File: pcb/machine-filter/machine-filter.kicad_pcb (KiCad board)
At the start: 2 copper layers, 150 x 107 mm, 162 parts, among them J1 PJ398SM, J10 PJ398SM, J11 PJ398SM, J12 PJ398SM, J13 EURO PWR 2x5, J14 EXPANSION 2x4, J15 TF-01A, J2 PJ398SM, J3 PJ398SM, J4 PJ398SM, J5 PJ398SM, J6 PJ398SM, J7 PJ398SM, J8 PJ398SM, J9 PJ398SM, U1 LMV324, U2 LMV324, U3 TL072, U4 TL072, U5 LM4040-10, U6 74HC4051, U7 LM324, U8 LM324

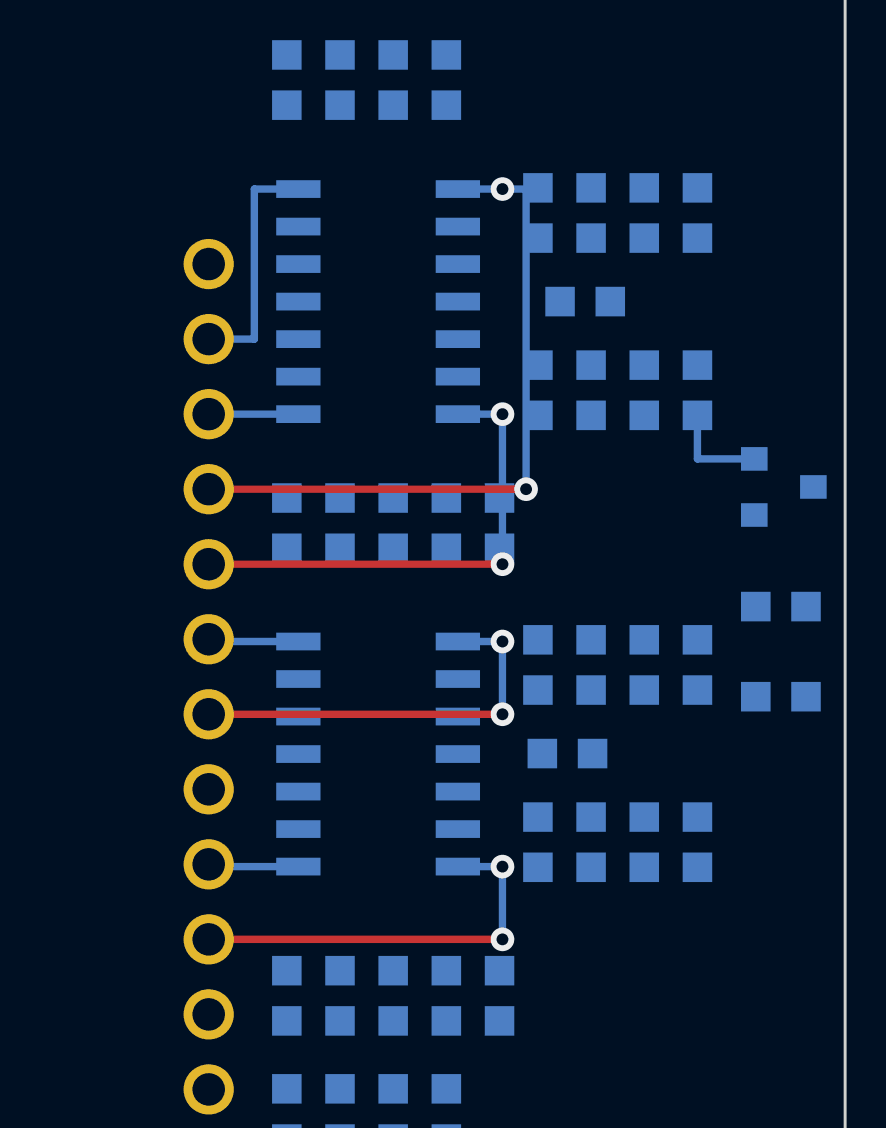
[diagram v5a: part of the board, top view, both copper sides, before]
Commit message: U1/U2 1.5 mm further from the Seed3 (d), C20/C21 with them; ADC traces redrawn; leftover vias removed
DRC: 0 problems (44 clashes with untraced minor parts ignored).

Co-Authored-By: Claude Opus 5.5 <noreply@anthropic.com>
Claude-Session: https://claude.ai/code/session_01Cf5qNBi3oNHhbCjPHvswth
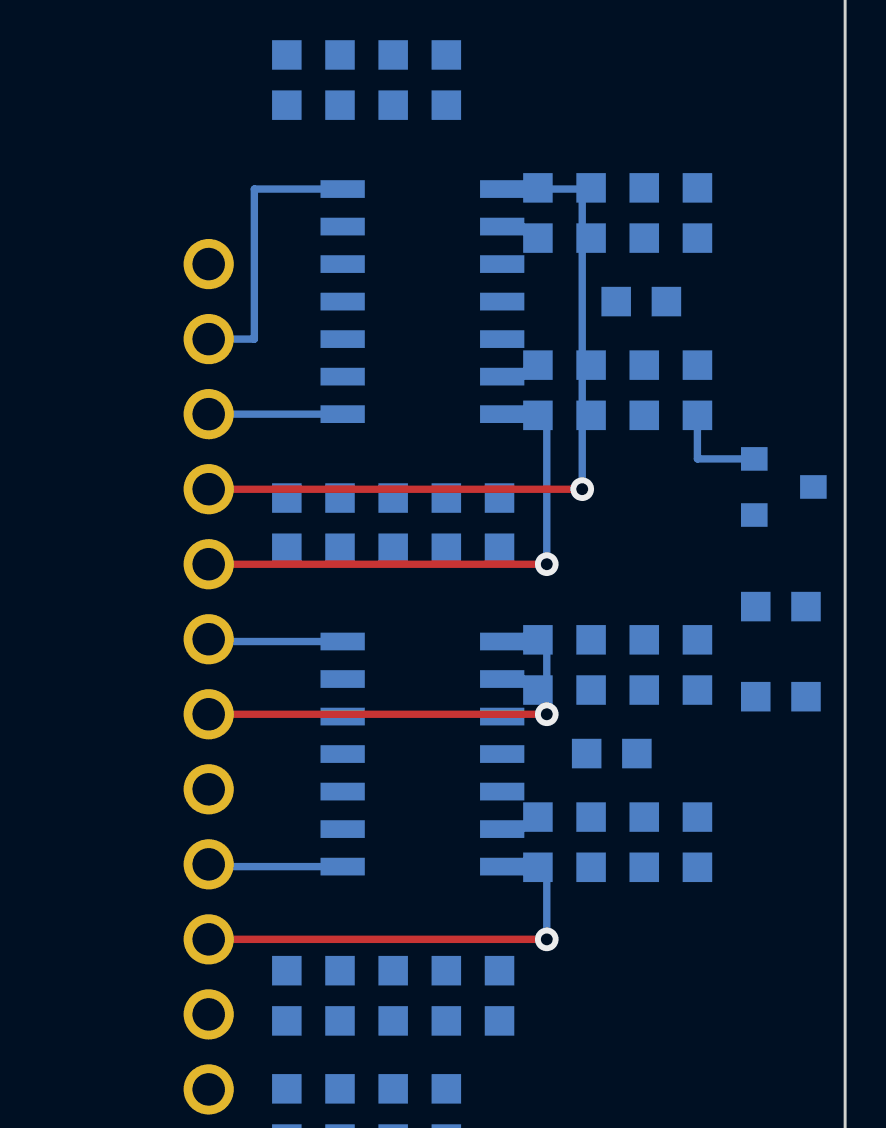
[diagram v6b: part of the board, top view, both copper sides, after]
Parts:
- moved C21 1.90 mm to (243.5, 92.5)
- moved C20 1.50 mm to (242.5, 107.8)
- moved U1 1.50 mm to (236.1, 107.8)
- moved U2 1.50 mm to (236.1, 92.5)
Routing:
- net ADC_LPRES: track 23.2 -> 25.5 mm, vias 2 -> 1
- net ADC_WIDTH: track 3.03 -> 4.53 mm
- net ADC_SRR: track 13.9 -> 15.4 mm, vias 2 -> 1
- net ADC_HPRES: track 8.11 -> 9.61 mm
- net ADC_EQG: track 3.03 -> 4.53 mm
- net ADC_EQF: track 16.5 -> 18.0 mm, vias 2 -> 1
- net ADC_DIST: track 13.9 -> 15.4 mm, vias 2 -> 1
- net ADC_BASE: track 3.04 -> 4.53 mm
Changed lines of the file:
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@@
 	(footprint "filter-module:SOIC-14_3.9x8.65mm_Pitch1.27mm"
 		(layer "B.Cu")
-		(at 234.6 92.493)
+		(at 236.1 92.493)
 		(descr "16-Lead Plastic Small Outline (SL) - Narrow, 3.90 mm Body [SOIC] (see Microchip Packaging Specification 00000049BS.pdf)")
 		(tags "SOIC 1.27")
@@
 	(footprint "filter-module:C_0603"
 		(layer "B.Cu")
-		(at 241 107.8)
+		(at 242.5 107.8)
 		(descr "Capacitor SMD 0603, reflow soldering, AVX (see smccp.pdf)")
 		(tags "capacitor 0603 C0603")
@@
 	(footprint "filter-module:SOIC-14_3.9x8.65mm_Pitch1.27mm"
 		(layer "B.Cu")
-		(at 234.6 107.81)
+		(at 236.1 107.81)
 		(descr "16-Lead Plastic Small Outline (SL) - Narrow, 3.90 mm Body [SOIC] (see Microchip Packaging Specification 00000049BS.pdf)")
 		(tags "SOIC 1.27")
@@
 	(footprint "filter-module:C_0603"
 		(layer "B.Cu")
-		(at 241.6 92.5)
+		(at 243.5 92.5)
 		(descr "Capacitor SMD 0603, reflow soldering, AVX (see smccp.pdf)")
 		(tags "capacitor 0603 C0603")
@@
 	)
 	(segment
-		(start 231.89 111.627)
+		(start 233.39 111.627)
 		(end 228.855 111.627)
 		(width 0.25)
@@
 	)
 	(segment
-		(start 231.89 96.310001)
+		(start 233.39 96.31)
 		(end 228.855 96.31)
 		(width 0.25)
@@
 	)
 	(segment
-		(start 239.6 98.85)
+		(start 241.5 98.85)
 		(end 228.855 98.85)
 		(width 0.25)
@@
 	)
 	(via
-		(at 238.8 88.69)
+		(at 241.5 98.85)
 		(size 0.8)
 		(drill 0.4)
@@
 		(net "ADC_LPRES")
 	)
-	(via
-		(at 239.6 98.85)
-		(size 0.8)
-		(drill 0.4)
-		(layers "F.Cu" "B.Cu")
-		(net "ADC_LPRES")
-	)
-	(segment
-		(start 239.6 88.69)
-		(end 239.6 98.85)
-		(width 0.25)
-		(layer "B.Cu")
-		(net "ADC_LPRES")
-	)
 	(segment
-		(start 238.8 88.69)
-		(end 239.6 88.69)
+		(start 241.5 88.69)
+		(end 241.5 98.85)
 		(width 0.25)
 		(layer "B.Cu")
@@
 	)
 	(segment
-		(start 237.29 88.69)
-		(end 238.8 88.69)
+		(start 238.79 88.69)
+		(end 241.5 88.69)
 		(width 0.25)
 		(layer "B.Cu")
@@
 	)
 	(segment
-		(start 231.89 88.69)
-		(end 230.4 88.69)
+		(start 230.4 88.69)
+		(end 230.4 93.77)
 		(width 0.25)
 		(layer "B.Cu")
@@
 	)
 	(segment
-		(start 230.4 88.69)
-		(end 230.4 93.77)
+		(start 230.4 93.77)
+		(end 228.855 93.77)
 		(width 0.25)
 		(layer "B.Cu")
@@
 	)
 	(segment
-		(start 230.4 93.77)
-		(end 228.855 93.77)
+		(start 233.39 88.69)
+		(end 230.4 88.69)
 		(width 0.25)
 		(layer "B.Cu")
@@
 	)
 	(segment
-		(start 238.8 101.39)
+		(start 240.3 101.39)
 		(end 228.855 101.39)
 		(width 0.25)
@@
 	)
 	(via
-		(at 238.8 101.39)
-		(size 0.8)
-		(drill 0.4)
-		(layers "F.Cu" "B.Cu")
-		(net "ADC_EQF")
-	)
-	(via
-		(at 238.8 96.31)
+		(at 240.3 101.39)
 		(size 0.8)
 		(drill 0.4)
@@
 	)
 	(segment
-		(start 237.29 96.31)
-		(end 238.8 96.31)
+		(start 238.79 96.31)
+		(end 240.3 96.31)
 		(width 0.25)
 		(layer "B.Cu")
@@
 	)
 	(segment
-		(start 238.8 96.31)
-		(end 238.8 101.39)
+		(start 240.3 96.31)
+		(end 240.3 101.39)
 		(width 0.25)
 		(layer "B.Cu")
@@
 	)
 	(segment
-		(start 231.89 104.007)
+		(start 233.39 104.007)
 		(end 228.855 104.007)
 		(width 0.25)
@@
 	)
 	(segment
-		(start 238.8 106.47)
+		(start 240.3 106.47)
 		(end 228.855 106.47)
 		(width 0.25)
@@
 	)
 	(via
-		(at 238.8 106.47)
-		(size 0.8)
-		(drill 0.4)
-		(layers "F.Cu" "B.Cu")
-		(net "ADC_DIST")
-	)
-	(via
-		(at 238.8 104.007)
+		(at 240.3 106.47)
 		(size 0.8)
 		(drill 0.4)
@@
 	)
 	(segment
-		(start 237.29 104.007)
-		(end 238.8 104.007)
+		(start 238.79 104.007)
+		(end 240.3 104.007)
 		(width 0.25)
 		(layer "B.Cu")
@@
 	)
 	(segment
-		(start 238.8 104.007)
-		(end 238.8 106.47)
+		(start 240.3 104.007)
+		(end 240.3 106.47)
 		(width 0.25)
 		(layer "B.Cu")
@@
 	)
 	(segment
-		(start 238.8 114.09)
+		(start 240.3 114.09)
 		(end 228.855 114.09)
 		(width 0.25)
@@
 	)
 	(via
-		(at 238.8 114.09)
-		(size 0.8)
-		(drill 0.4)
-		(layers "F.Cu" "B.Cu")
-		(net "ADC_SRR")
-	)
-	(via
-		(at 238.8 111.627)
+		(at 240.3 114.09)
 		(size 0.8)
 		(drill 0.4)
@@
 	)
 	(segment
-		(start 238.8 111.627)
-		(end 238.8 114.09)
+		(start 238.79 111.627)
+		(end 240.3 111.627)
 		(width 0.25)
 		(layer "B.Cu")
@@
 	)
 	(segment
-		(start 237.29 111.627)
-		(end 238.8 111.627)
+		(start 240.3 111.627)
+		(end 240.3 114.09)
 		(width 0.25)
 		(layer "B.Cu")

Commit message: Op-amps rotated 90 deg each toward the Seed3 (d); J13 upright with its block re-packed; J14 upright by the edge; traces redrawn
- U2/U1 clockwise, U3/U4 counter-clockwise (by which keeps more Seed3-connected
  pins near it); konnect_place.py picks the KiCad angle by where pad 1 lands.
- Eight ADC traces redrawn; old vias removed with kicad-python (by net, and one
  re-netted via by position).
- Power block packed beside the upright header (fits: 31 x 23 mm).
- J14 upright at x 64.6; USB D-/D+ redrawn.
DRC: 0 problems (50 clashes with untraced minor parts ignored).

Co-Authored-By: Claude Opus 5.5 <noreply@anthropic.com>
Claude-Session: https://claude.ai/code/session_01Cf5qNBi3oNHhbCjPHvswth
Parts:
- moved C1 20.0 mm to (207.2, 136.9)
- moved D10 20.0 mm to (201.7, 136.9)
- moved C3 14.0 mm to (202.3, 149.0)
- moved D11 14.0 mm to (196.8, 149.0)
- moved FB1 11.5 mm to (196.2, 137.0)
- moved J14 8.49 mm to (244.6, 133.1), turned to 180 degrees
- moved J13 8.10 mm to (188.0, 146.7), turned to 180 degrees
- moved C2 8.02 mm to (199.2, 143.0)
- moved FB2 8.02 mm to (207.1, 140.4)
- moved C4 4.68 mm to (199.2, 155.0)
- moved C20 1.00 mm to (243.5, 107.8)
- turned U1 to -90 degrees
- turned U2 to -90 degrees
- turned U3 to 90 degrees
- turned U4 to 90 degrees
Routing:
- net ADC_EQG: track 4.53 -> 14.4 mm, vias 0 -> 1
- net ADC_SRR: track 15.4 -> 7.02 mm, vias 1 -> 0
- net ADC_EQF: track 18.0 -> 9.63 mm, vias 1 -> 0
- net /Main: Daisy Seed3/USB_DP: track 11.5 -> 19.6 mm
- net ADC_HPRES: track 9.61 -> 17.2 mm, vias 0 -> 1
- net ADC_LPRES: track 25.5 -> 18.1 mm
- net ADC_BASE: track 4.53 -> 9.95 mm
- net ADC_WIDTH: track 4.53 -> 9.88 mm
- net ADC_DIST: track 15.4 -> 18.5 mm
- net Net-(FB1-Pad1): track 10.6 -> 13.2 mm

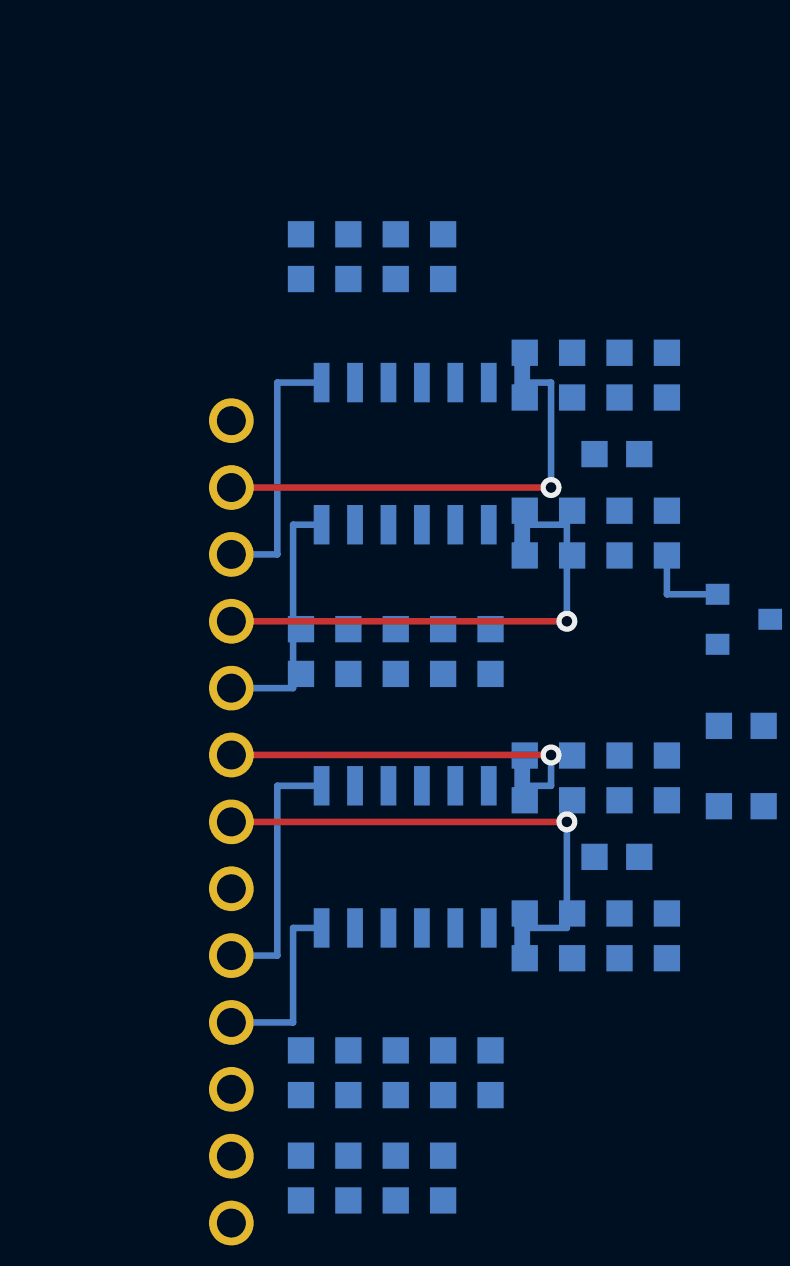
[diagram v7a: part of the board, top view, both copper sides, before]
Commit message: Input resistors R10/R13 (BASE), R18 (HP RES), R14/R17 (WIDTH) in line with their op-amp pins; straight traces (d)
Co-Authored-By: Claude Opus 5.5 <noreply@anthropic.com>
Claude-Session: https://claude.ai/code/session_01Cf5qNBi3oNHhbCjPHvswth
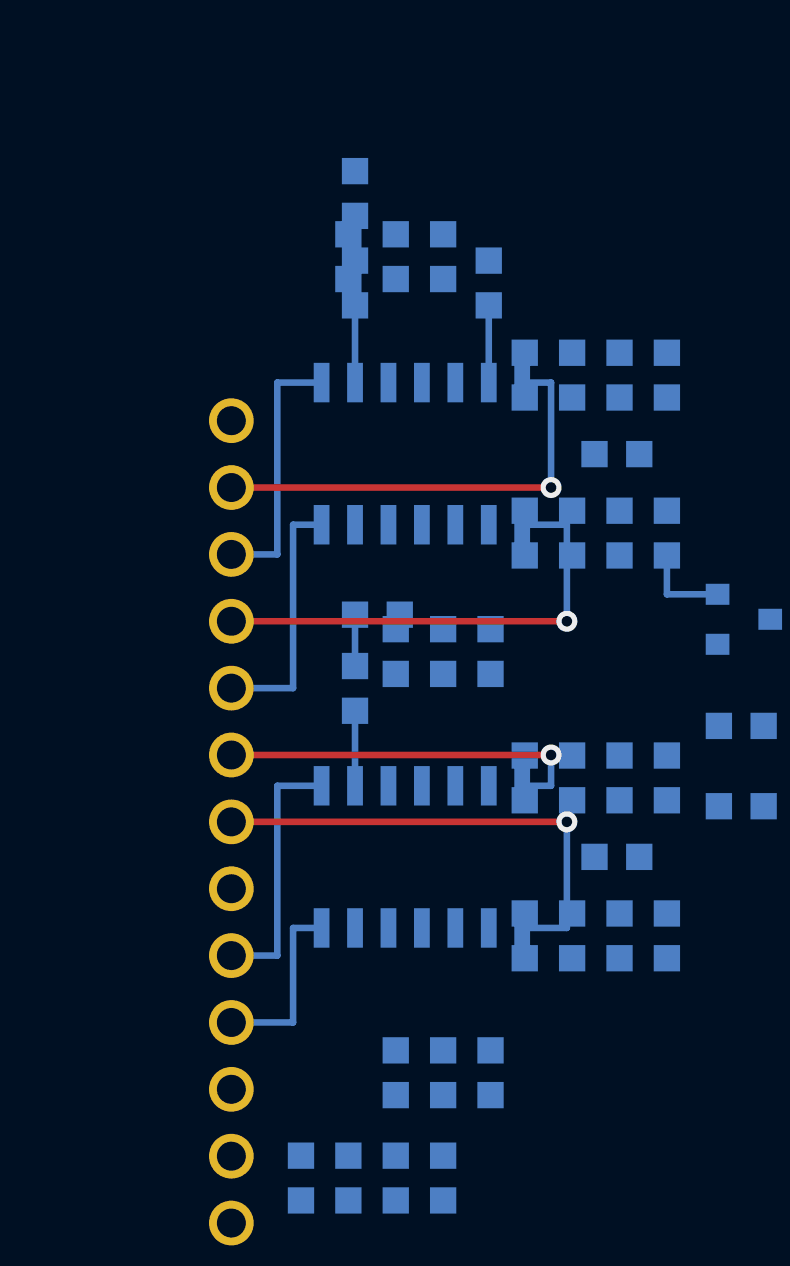
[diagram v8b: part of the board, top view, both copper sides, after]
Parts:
- moved R14 17.6 mm to (234.4, 98.6), turned to 180 degrees
- moved R10 17.5 mm to (233.6, 82.6)
- moved R17 14.6 mm to (233.6, 101.4), turned to -90 degrees
- moved R13 14.0 mm to (233.6, 86.0)
- moved R18 7.20 mm to (238.6, 86.0)
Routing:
- net Net-(U2B--): track 0.00 -> 2.93 mm
- net Net-(U2A--): track 0.00 -> 2.93 mm
- net Net-(U1A--): track 0.00 -> 2.85 mm
- net Net-(R14-Pad2): track 0.00 -> 1.95 mm
- net Net-(R10-Pad2): track 0.00 -> 1.70 mm
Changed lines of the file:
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@@
 	(footprint "filter-module:R_0603"
 		(layer "B.Cu")
-		(at 231.5 100 -90)
+		(at 233.553 82.6 -90)
 		(descr "Resistor SMD 0603, reflow soldering, Vishay (see dcrcw.pdf)")
 		(tags "resistor 0603")
@@
 	(footprint "filter-module:R_0603"
 		(layer "B.Cu")
-		(at 231.5 116 90)
+		(at 234.403 98.6 180)
 		(descr "Resistor SMD 0603, reflow soldering, Vishay (see dcrcw.pdf)")
 		(tags "resistor 0603")
 		(property "Reference" "R14"
-			(at 0 1.449999 270)
+			(at 0 1.449999 0)
 			(unlocked yes)
 			(layer "B.SilkS")
@@
 		)
 		(property "Value" "100k 0.1%"
-			(at 0 -1.45 270)
+			(at 0 -1.45 0)
 			(unlocked yes)
 			(layer "B.SilkS")
@@
 		)
 		(property "Datasheet" ""
-			(at 0 0 270)
+			(at 0 0 0)
 			(layer "B.Fab")
 			(hide yes)
@@
 		)
 		(property "Description" ""
-			(at 0 0 270)
+			(at 0 0 0)
 			(layer "B.Fab")
 			(hide yes)
@@
 		)
 		(fp_line
-			(start -1.6 -0.75)
+			(start 1.6 0.75)
 			(end 1.6 -0.75)
 			(stroke
@@
 		)
 		(fp_line
-			(start 1.6 0.75)
-			(end 1.6 -0.75)
+			(start -1.6 0.75)
+			(end 1.6 0.75)
 			(stroke
 				(width 0.05)
@@
 		)
 		(fp_line
-			(start -1.6 0.75)
-			(end 1.6 0.75)
+			(start -1.6 -0.75)
+			(end 1.6 -0.75)
 			(stroke
 				(width 0.05)
@@
 		)
 		(pad "1" smd rect
-			(at -0.85 0 90)
+			(at -0.85 0 180)
 			(size 1 1)
 			(layers "B.Cu" "B.Mask" "B.Paste")
@@
 		)
 		(pad "2" smd rect
-			(at 0.85 0 90)
+			(at 0.85 0 180)
 			(size 1 1)
 			(layers "B.Cu" "B.Mask" "B.Paste")
@@
 	(footprint "filter-module:R_0603"
 		(layer "B.Cu")
-		(at 233.3 100 -90)
+		(at 233.553 86 -90)
 		(descr "Resistor SMD 0603, reflow soldering, Vishay (see dcrcw.pdf)")
 		(tags "resistor 0603")
@@
 	(footprint "filter-module:R_0603"
 		(layer "B.Cu")
-		(at 231.5 85 -90)
+		(at 238.633 86 -90)
 		(descr "Resistor SMD 0603, reflow soldering, Vishay (see dcrcw.pdf)")
 		(tags "resistor 0603")
@@
 	(footprint "filter-module:R_0603"
 		(layer "B.Cu")
-		(at 233.3 116 90)
+		(at 233.553 101.4 -90)
 		(descr "Resistor SMD 0603, reflow soldering, Vishay (see dcrcw.pdf)")
 		(tags "resistor 0603")
 		(property "Reference" "R17"
-			(at 0 1.449999 270)
+			(at 0 1.449999 90)
 			(unlocked yes)
 			(layer "B.SilkS")
@@
 		)
 		(property "Value" "20k 0.1%"
-			(at 0 -1.45 270)
+			(at 0 -1.45 90)
 			(unlocked yes)
 			(layer "B.SilkS")
@@
 		)
 		(property "Datasheet" ""
-			(at 0 0 270)
+			(at 0 0 90)
 			(layer "B.Fab")
 			(hide yes)
@@
 		)
 		(property "Description" ""
-			(at 0 0 270)
+			(at 0 0 90)
 			(layer "B.Fab")
 			(hide yes)
@@
 		(duplicate_pad_numbers_are_jumpers no)
 		(fp_line
-			(start 0.85 -0.7)
-			(end -0.85 -0.7)
+			(start -0.85 0.699999)
+			(end 0.85 0.699999)
 			(stroke
 				(width 0.12)
@@
 		)
 		(fp_line
-			(start -0.85 0.699999)
-			(end 0.85 0.699999)
+			(start 0.85 -0.7)
+			(end -0.85 -0.7)
 			(stroke
 				(width 0.12)
@@
 		)
 		(fp_line
-			(start -1.6 -0.75)
-			(end 1.6 -0.75)
+			(start -1.6 0.75)
+			(end 1.6 0.75)
 			(stroke
 				(width 0.05)
@@
 		)
 		(fp_line
-			(start 1.6 0.75)
-			(end 1.6 -0.75)
+			(start -1.6 0.75)
+			(end -1.6 -0.75)
 			(stroke
 				(width 0.05)
@@
 		)
 		(fp_line
-			(start -1.6 0.75)
-			(end -1.6 -0.75)
+			(start 1.6 0.75)
+			(end 1.6 -0.75)
 			(stroke
 				(width 0.05)
@@
 		)
 		(fp_line
-			(start -1.6 0.75)
-			(end 1.6 0.75)
+			(start -1.6 -0.75)
+			(end 1.6 -0.75)
 			(stroke
 				(width 0.05)
@@
 		)
 		(pad "1" smd rect
-			(at -0.85 0 90)
+			(at -0.85 0 270)
 			(size 1 1)
 			(layers "B.Cu" "B.Mask" "B.Paste")
@@
 		)
 		(pad "2" smd rect
-			(at 0.85 0 90)
+			(at 0.85 0 270)
 			(size 1 1)
 			(layers "B.Cu" "B.Mask" "B.Paste")
@@
 	)
 	(segment
+		(start 233.553 86.85)
+		(end 233.553 89.783)
+		(width 0.25)
+		(layer "B.Cu")
+		(net "Net-(U2A--)")
+	)
+	(segment
+		(start 238.633 86.85)
+		(end 238.633 89.783)
+		(width 0.25)
+		(layer "B.Cu")
+		(net "Net-(U2B--)")
+	)
+	(segment
 		(start 247.325 97.825)
 		(end 245.4 97.825)
@@
 	)
 	(segment
+		(start 233.553 83.45)
+		(end 233.553 85.15)
+		(width 0.25)
+		(layer "B.Cu")
+		(net "Net-(R10-Pad2)")
+	)
+	(segment
+		(start 233.553 102.25)
+		(end 233.553 105.1)
+		(width 0.25)
+		(layer "B.Cu")
+		(net "Net-(U1A--)")
+	)
+	(segment
 		(start 195.2175 141.624999)
 		(end 195.2175 136.975)
@@
 		(net "Net-(FB1-Pad1)")
 	)
+	(segment
+		(start 233.553 98.6)
+		(end 233.553 100.55)
+		(width 0.25)
+		(layer "B.Cu")
+		(net "Net-(R14-Pad2)")
+	)
 	(embedded_fonts no)
